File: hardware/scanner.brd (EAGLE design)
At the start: 65 x 56 mm, 24 parts, among them U1 CAT24C32WI-GT3, U2 TPS61165DBV

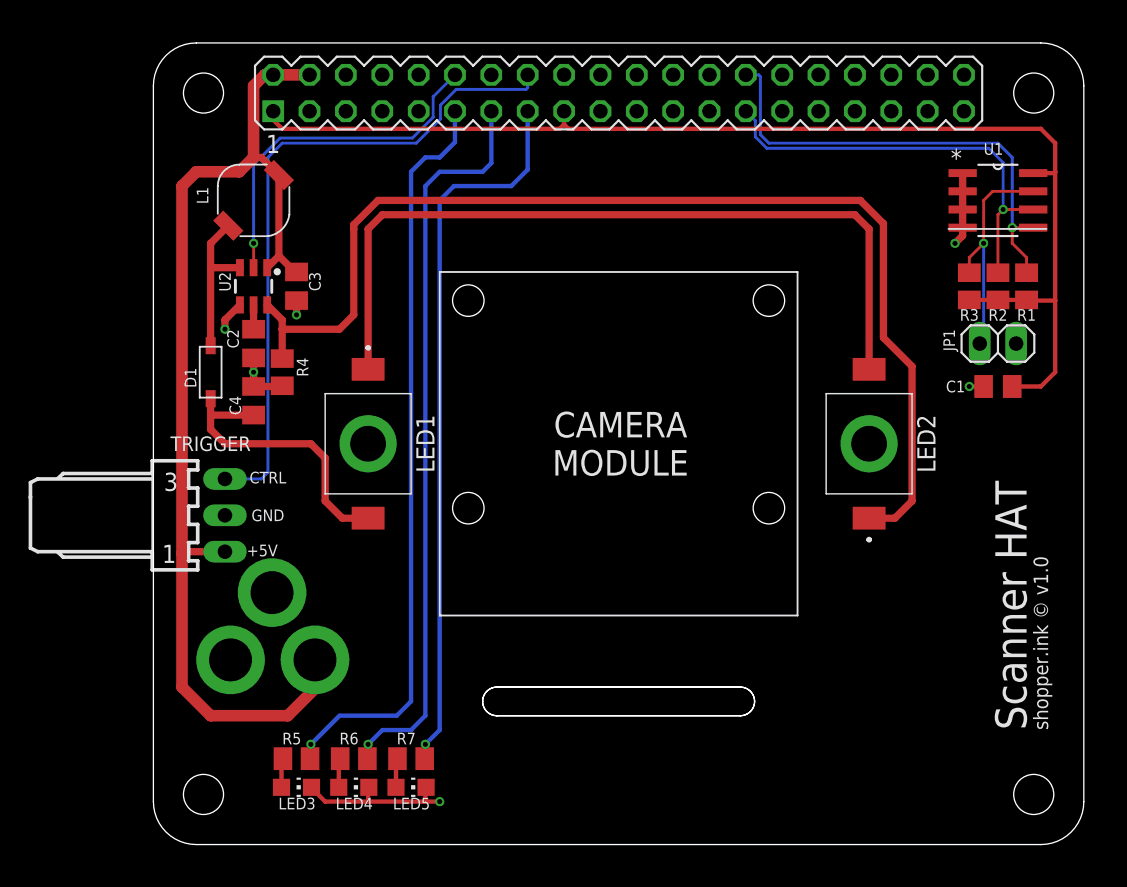
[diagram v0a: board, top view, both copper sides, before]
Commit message: redo eeprom area
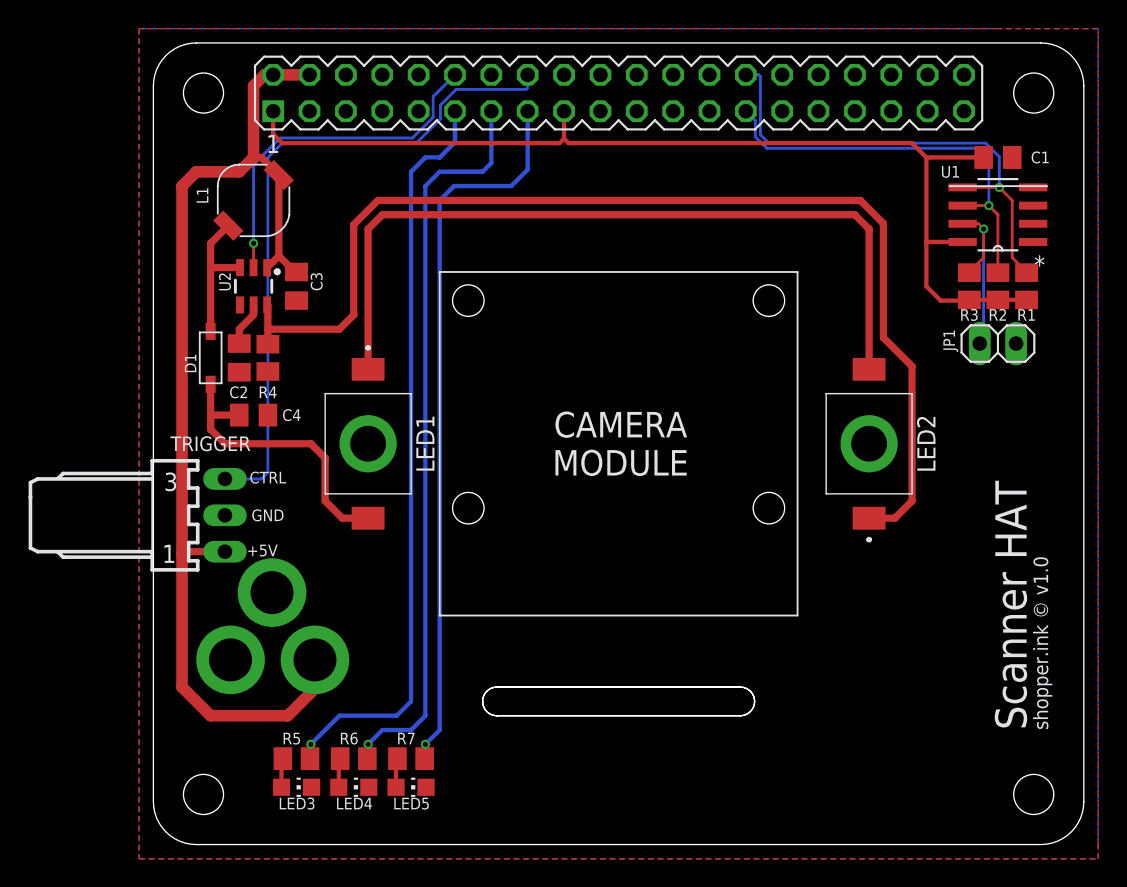
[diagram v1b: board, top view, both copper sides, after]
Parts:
- moved C1 16.0 mm to (59.0, 48.0), turned to 0 degrees
- moved C2 1.41 mm to (6.00, 34.0)
- moved R4 1.41 mm to (8.00, 34.0)
- moved C4 1.00 mm to (7.00, 30.0), turned to 0 degrees
- moved D1 1.00 mm to (4.00, 34.0)
- moved U1 1.00 mm to (59.0, 44.0), turned to 180 degrees
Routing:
- net GND: track 24.7 -> 0.19 mm, vias 6 -> 0
- net +3V3: track 84.6 -> 73.1 mm
- net EEPROM_WP: track 16.3 -> 13.2 mm
- net N$7: track 1.70 -> 3.11 mm
- net LED_SW: track 10.9 -> 9.94 mm
- net EEPROM_SCL: track 30.1 -> 29.3 mm
- added copper zone on layer 1, net GND
- added copper zone on layer 15, net GND
- added copper zone on layer 16, net GND

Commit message: .
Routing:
- net EEPROM_SDA: track 33.9 -> 33.2 mm
- net TRIGGER: track 46.8 -> 46.3 mm
- removed copper zone on layer 15, net GND
- removed copper zone on layer 2, net GND
